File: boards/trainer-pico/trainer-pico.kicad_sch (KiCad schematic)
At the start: 38 parts, among them J1 Conn_01x08_Pin, J10 Conn_01x04_Socket, J11 Conn_01x17_Pin, J12 Conn_01x17_Socket, J13 Conn_01x17_Socket, J14 Conn_01x17_Pin, J15 Barrel_Jack_Switch, J16 Conn_01x04_Pin, J17 Conn_01x04_Pin, J18 Conn_01x04_Pin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

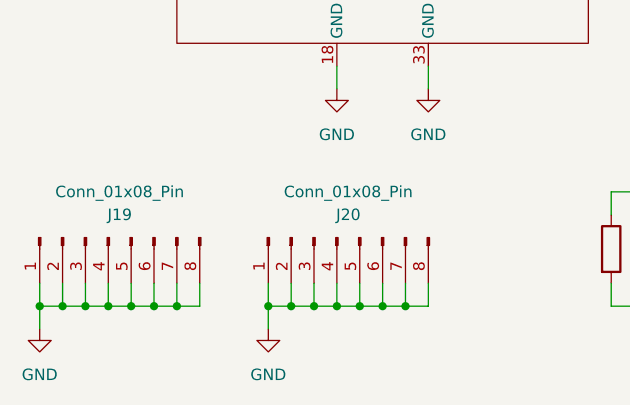
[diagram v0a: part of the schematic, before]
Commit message: サブ基板の固定方法を変更
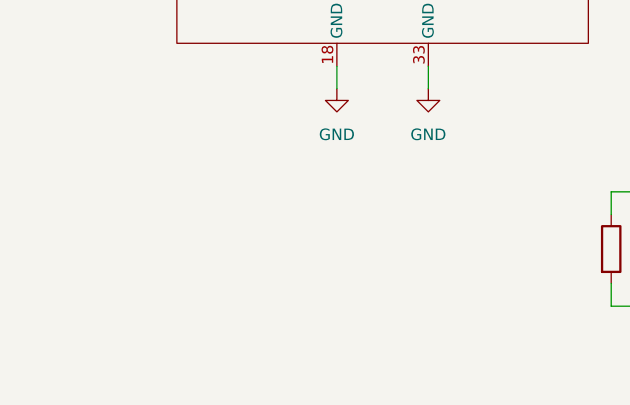
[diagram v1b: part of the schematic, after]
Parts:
- removed J19, J20: Conn_01x08_Pin, Connector_PinSocket_2.54mm:PinSocket_1x08_P2.54mm_Vertical, symbol Connector:Conn_01x08_Pin
